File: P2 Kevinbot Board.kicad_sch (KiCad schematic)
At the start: 57 parts, among them J1 Screw_Terminal_01x02, J10 Conn_01x04, J11 Conn_01x04_Male, J12 Conn_02x06_Odd_Even, J13 Conn_01x04, J14 Conn_01x02, J15 Conn_01x04, J16 Conn_02x06_Odd_Even, J2 Conn_01x03_Male, J3 Screw_Terminal_01x02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

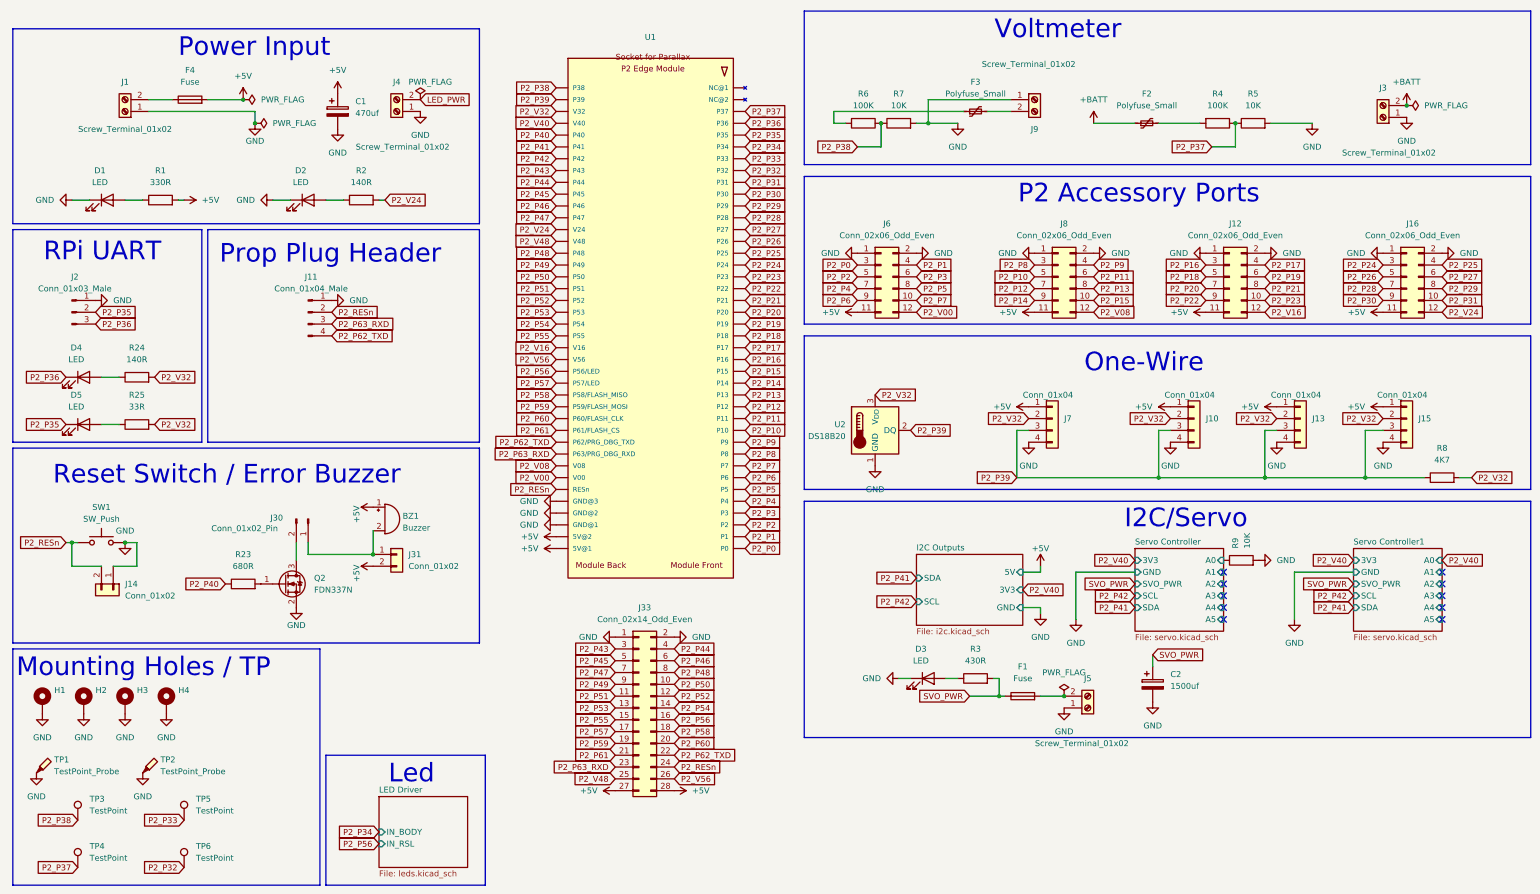
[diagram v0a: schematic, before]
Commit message: Remove all components, redo board outline
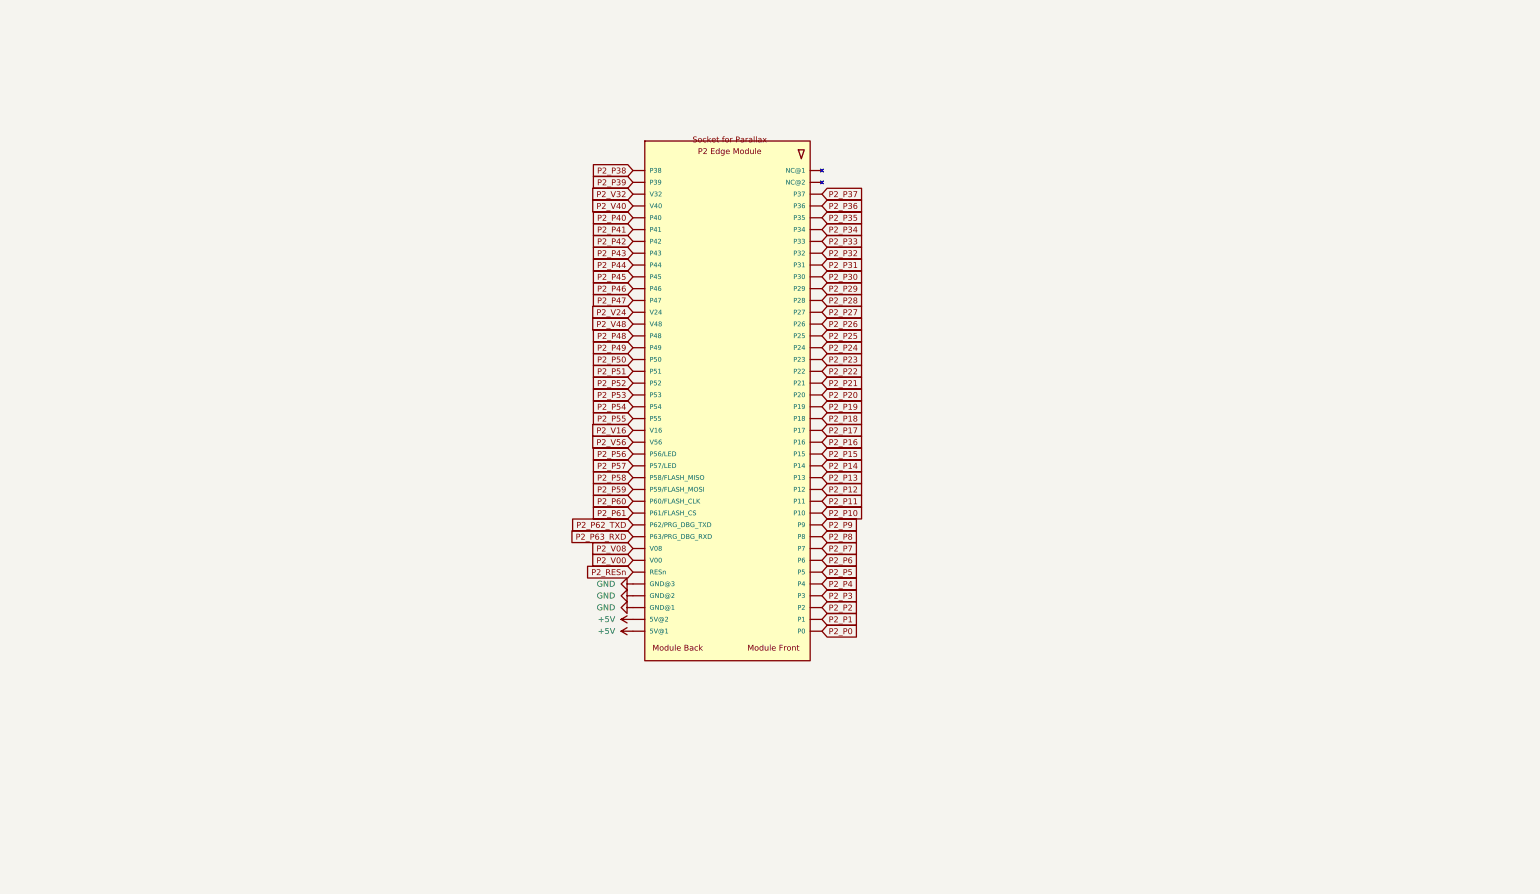
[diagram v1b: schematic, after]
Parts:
- removed BZ1: Buzzer, Buzzer_Beeper:Buzzer_TDK_PS1240P02BT_D12.2mm_H6.5mm, symbol Device:Buzzer
- removed C1: 470uf, Capacitor_THT:CP_Radial_D8.0mm_P3.50mm, symbol Device:C_Polarized
- removed C2: 1500uf, Capacitor_THT:CP_Radial_D8.0mm_P3.50mm, symbol Device:C_Polarized
- removed D1, D2, D3, D4, D5: LED, LED_SMD:LED_0805_2012Metric, symbol Device:LED
- removed F1, F4: Fuse, Fuse:Fuseholder_Blade_Mini_Keystone_3568, symbol Device:Fuse
- removed F2, F3: Polyfuse_Small, Fuse:Fuse_1206_3216Metric_Pad1.42x1.75mm_HandSolder, symbol Device:Polyfuse_Small
- removed H1, H2, H3, H4: MountingHole_Pad, MountingHole:MountingHole_3.5mm_Pad_TopBottom, symbol Mechanical:MountingHole_Pad
- removed J1, J3, J4, J5, J9: Screw_Terminal_01x02, Phoenix_MSTBA:MSTBA-2,5-2-G-5,08, symbol Connector:Screw_Terminal_01x02
- removed J10, J13, J15, J7: Conn_01x04, Connector_JST:JST_XH_B4B-XH-A_1x04_P2.50mm_Vertical, symbol Connector_Generic:Conn_01x04
- removed J11: Conn_01x04_Male, Connector_PinHeader_2.54mm:PinHeader_1x04_P2.54mm_Vertical, symbol Connector:Conn_01x04_Pin
- removed J12, J16, J6, J8: Conn_02x06_Odd_Even, Connector_PinHeader_2.54mm:PinHeader_2x06_P2.54mm_Vertical, symbol Connector_Generic:Conn_02x06_Odd_Even
- removed J14, J31: Conn_01x02, Connector_JST:JST_XH_B2B-XH-A_1x02_P2.50mm_Vertical, symbol Connector_Generic:Conn_01x02
- removed J2: Conn_01x03_Male, Connector_JST:JST_XH_B3B-XH-A_1x03_P2.50mm_Vertical, symbol Connector:Conn_01x03_Pin
- removed J30: Conn_01x02_Pin, Connector_PinHeader_2.54mm:PinHeader_1x02_P2.54mm_Vertical, symbol Connector:Conn_01x02_Pin
- removed J33: Conn_02x14_Odd_Even, Connector_FFC-FPC:TE_2-1734839-8_1x28-1MP_P0.5mm_Horizontal, symbol Connector_Generic:Conn_02x14_Odd_Even
- removed Q2: FDN337N, Package_TO_SOT_SMD:SOT-23-3, symbol Device:Q_NMOS_GSD
- removed R1: 330R, Resistor_SMD:R_0805_2012Metric, symbol Device:R
- removed R2, R24: 140R, Resistor_SMD:R_0805_2012Metric, symbol Device:R
- removed R23: 680R, Resistor_SMD:R_0603_1608Metric, symbol Device:R
- removed R25: 33R, Resistor_SMD:R_0805_2012Metric, symbol Device:R
- removed R3: 430R, Resistor_SMD:R_0805_2012Metric, symbol Device:R
- removed R4, R6: 100K, Resistor_THT:R_Axial_DIN0207_L6.3mm_D2.5mm_P10.16mm_Horizontal, symbol Device:R
- removed R5, R7: 10K, Resistor_THT:R_Axial_DIN0207_L6.3mm_D2.5mm_P10.16mm_Horizontal, symbol Device:R
- removed R8: 4K7, Resistor_SMD:R_0603_1608Metric, symbol Device:R
- removed R9: 10K, Resistor_SMD:R_0603_1608Metric, symbol Device:R
- removed SW1: SW_Push, Button_Switch_THT:SW_PUSH_6mm, symbol Switch:SW_Push
- removed TP1, TP2: TestPoint_Probe, Keystone:Keystone-1502-2, symbol Connector:TestPoint_Probe
- removed TP3, TP4, TP5, TP6: TestPoint, TestPoint:TestPoint_Pad_D1.0mm, symbol Connector:TestPoint
- removed U2: DS18B20, Package_TO_SOT_THT:TO-92_Inline_Wide, symbol Sensor_Temperature:DS18B20
- U1: footprint Parallax-P2:Card_Edge_SMT_VERT_1.27mm_80p -> Parallax-P2:Card_Edge_TH_RA_1.27mm_80p; Part Number 450-00309 -> (none)
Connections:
- no-connect marks 10 -> 0
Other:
- removed sheet I2C Outputs
- removed sheet LED Driver
- removed sheet Servo Controller
- removed sheet Servo Controller1
- note removed: "I2C/Servo"
- note removed: "Led"
- note removed: "Mounting Holes / TP"
- note removed: "One-Wire"
- note removed: "P2 Accessory Ports"
- note removed: "Power Input"
- note removed: "Prop Plug Header"
- note removed: "RPi UART"
- note removed: "Reset Switch / Error Buzzer"
- note removed: "Voltmeter"

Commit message: Mostly routed accessory headers
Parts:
- added J12, J16, J6, J8: Conn_02x06_Odd_Even, Connector_PinHeader_2.54mm:PinHeader_2x06_P2.54mm_Vertical, symbol Connector_Generic:Conn_02x06_Odd_Even
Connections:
- net +5V: now also J12.11 (Pin_11), J16.11 (Pin_11), J6.11 (Pin_11), J8.11 (Pin_11)
- net GND: now also J12.1 (Pin_1), J12.2 (Pin_2), J16.1 (Pin_1), J16.2 (Pin_2), J6.1 (Pin_1), J6.2 (Pin_2), J8.1 (Pin_1), J8.2 (Pin_2)
- net P2_P0: now also J6.3 (Pin_3)
- net P2_P1: now also J6.4 (Pin_4)
- net P2_P10: now also J8.5 (Pin_5)
- net P2_P11: now also J8.6 (Pin_6)
- net P2_P12: now also J8.7 (Pin_7)
- net P2_P13: now also J8.8 (Pin_8)
- net P2_P14: now also J8.9 (Pin_9)
- net P2_P15: now also J8.10 (Pin_10)
- net P2_P16: now also J12.3 (Pin_3)
- net P2_P17: now also J12.4 (Pin_4)
- net P2_P18: now also J12.5 (Pin_5)
- net P2_P19: now also J12.6 (Pin_6)
- net P2_P2: now also J6.5 (Pin_5)
- net P2_P20: now also J12.7 (Pin_7)
- net P2_P21: now also J12.8 (Pin_8)
- net P2_P22: now also J12.9 (Pin_9)
- net P2_P23: now also J12.10 (Pin_10)
- net P2_P24: now also J16.3 (Pin_3)
- net P2_P25: now also J16.4 (Pin_4)
- net P2_P26: now also J16.5 (Pin_5)
- net P2_P27: now also J16.6 (Pin_6)
- net P2_P28: now also J16.7 (Pin_7)
- net P2_P29: now also J16.8 (Pin_8)
- net P2_P3: now also J6.6 (Pin_6)
- net P2_P30: now also J16.9 (Pin_9)
- net P2_P31: now also J16.10 (Pin_10)
- net P2_P4: now also J6.7 (Pin_7)
- net P2_P5: now also J6.8 (Pin_8)
- net P2_P6: now also J6.9 (Pin_9)
- net P2_P7: now also J6.10 (Pin_10)
- net P2_P8: now also J8.3 (Pin_3)
- net P2_P9: now also J8.4 (Pin_4)
- net P2_V00: now also J6.12 (Pin_12)
- net P2_V08: now also J8.12 (Pin_12)
- net P2_V16: now also J12.12 (Pin_12)
- net P2_V24: now also J16.12 (Pin_12)

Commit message: Begin work on usbc programmer, misc
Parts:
- added J1, J2: Conn_01x03_Pin, Connector_PinHeader_2.54mm:PinHeader_1x03_P2.54mm_Vertical, symbol Connector:Conn_01x03_Pin
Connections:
- net +5V: now also J1.1 (Pin_1), J2.1 (Pin_1); no longer J12.11 (Pin_11), J16.11 (Pin_11), J6.11 (Pin_11), J8.11 (Pin_11)
- new net: J12.11 (Pin_11), J16.11 (Pin_11), J2.2 (Pin_2)
- new net: J1.2 (Pin_2), J6.11 (Pin_11), J8.11 (Pin_11)
- no-connect marks 0 -> 2
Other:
- added sheet Programmer (prog.kicad_sch)

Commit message: Usb programme
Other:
- sheet Programmer ports: added RESn, RX, TX; removed none
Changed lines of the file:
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@@
 	(wire
 		(pts
+			(xy 39.37 147.32) (xy 49.53 147.32)
+		)
+		(stroke
+			(width 0)
+			(type default)
+		)
+	)
+	(wire
+		(pts
 			(xy 171.45 147.32) (xy 171.45 158.75)
 		)
@@
 	(wire
 		(pts
+			(xy 162.56 88.9) (xy 163.83 88.9)
+		)
+		(stroke
+			(width 0)
+			(type default)
+		)
+	)
+	(wire
+		(pts
 			(xy 284.48 147.32) (xy 284.48 130.81)
 		)
@@
 		)
 	)
+	(label "P2_RESn"
+		(at 162.56 88.9 180)
+		(effects
+			(font
+				(size 1.27 1.27)
+			)
+			(justify right bottom)
+		)
+	)
+	(label "P2_RESn"
+		(at 39.37 147.32 180)
+		(effects
+			(font
+				(size 1.27 1.27)
+			)
+			(justify right bottom)
+		)
+	)
 	(global_label "P2_P31"
 		(shape input)
@@
 		)
 	)
-	(global_label "P2_RESn"
-		(shape input)
-		(at 49.53 147.32 180)
-		(fields_autoplaced yes)
-		(effects
-			(font
-				(size 1.27 1.27)
-			)
-			(justify right)
-		)
-		(property "Intersheetrefs" "${INTERSHEET_REFS}"
-			(at 38.8921 147.2406 0)
-			(effects
-				(font
-					(size 1.27 1.27)
-				)
-				(justify right)
-				(hide yes)
-			)
-		)
-	)
 	(global_label "P2_P16"
 		(shape input)
@@
 		)
 	)
+	(global_label "P2_P62_TXD"
+		(shape input)
+		(at 163.83 91.44 180)
+		(fields_autoplaced yes)
+		(effects
+			(font
+				(size 1.27 1.27)
+			)
+			(justify right)
+		)
+		(property "Intersheetrefs" "${INTERSHEET_REFS}"
+			(at 149.8659 91.5194 0)
+			(effects
+				(font
+					(size 1.27 1.27)
+				)
+				(justify right)
+				(hide yes)
+			)
+		)
+	)
+	(global_label "P2_P63_RXD"
+		(shape input)
+		(at 163.83 93.98 180)
+		(fields_autoplaced yes)
+		(effects
+			(font
+				(size 1.27 1.27)
+			)
+			(justify right)
+		)
+		(property "Intersheetrefs" "${INTERSHEET_REFS}"
+			(at 149.5636 94.0594 0)
+			(effects
+				(font
+					(size 1.27 1.27)
+				)
+				(justify right)
+				(hide yes)
+			)
+		)
+	)
 	(global_label "P2_P7"
 		(shape input)
@@
 	)
 	(sheet
-		(at 185.42 171.45)
-		(size 36.83 16.51)
+		(at 163.83 83.82)
+		(size 20.32 15.24)
 		(exclude_from_sim no)
 		(in_bom yes)
@@
 		)
 		(property "Sheetname" "Programmer"
-			(at 185.42 170.7384 0)
+			(at 163.83 83.1084 0)
 			(effects
 				(font
@@
 		)
 		(property "Sheetfile" "prog.kicad_sch"
-			(at 185.42 188.5446 0)
+			(at 163.83 99.6446 0)
 			(effects
 				(font
@@
 			)
 		)
+		(pin "RESn" input
+			(at 163.83 88.9 180)
+			(effects
+				(font
+					(size 1.27 1.27)
+				)
+				(justify left)
+			)
+		)
+		(pin "RX" input
+			(at 163.83 91.44 180)
+			(effects
+				(font
+					(size 1.27 1.27)
+				)
+				(justify left)
+			)
+		)
+		(pin "TX" input
+			(at 163.83 93.98 180)
+			(effects
+				(font
+					(size 1.27 1.27)
+				)
+				(justify left)
+			)
+		)

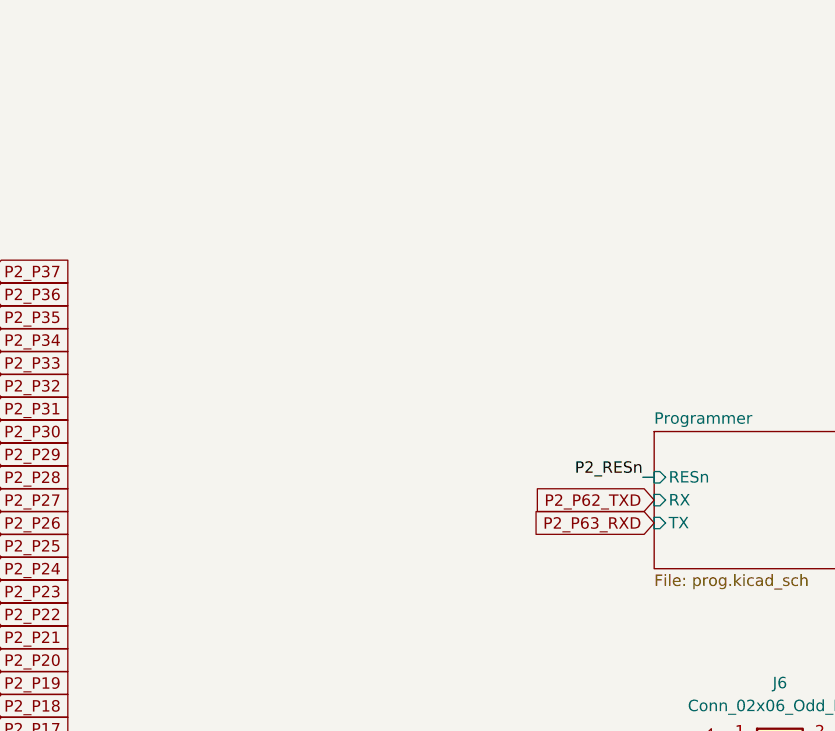
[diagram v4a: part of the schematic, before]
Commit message: Place buzzer
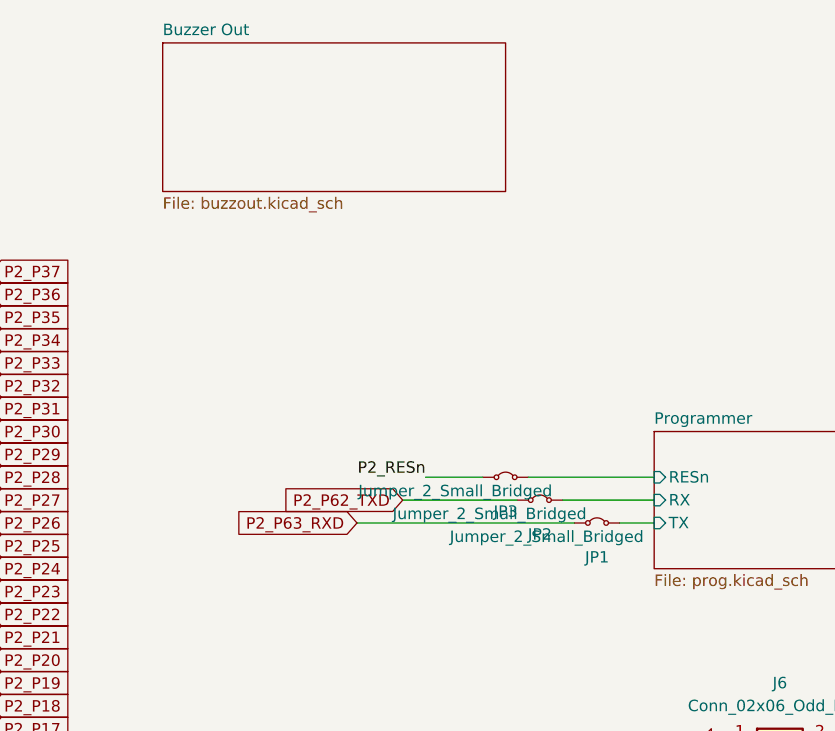
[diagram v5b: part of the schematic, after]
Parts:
- added JP1, JP2, JP3: Jumper_2_Small_Bridged, Jumper:SolderJumper-2_P1.3mm_Bridged_RoundedPad1.0x1.5mm, symbol Jumper:Jumper_2_Small_Bridged
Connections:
- net P2_P62_TXD: now also JP2.1 (A)
- net P2_P63_RXD: now also JP1.1 (A)
- net P2_RESn: now also JP3.1 (A)
- new net Programmer/RESn: JP3.2 (B)
- new net Programmer/RX: JP2.2 (B)
- new net Programmer/TX: JP1.2 (B)
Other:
- added sheet Buzzer Out (buzzout.kicad_sch)

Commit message: Buzzer
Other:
- sheet Buzzer Out ports: added SIG, VIN; removed none
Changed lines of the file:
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@@
+		)
+	)
+	(global_label "P2_P34"
+		(shape input)
+		(at 163.83 68.58 180)
+		(fields_autoplaced yes)
+		(effects
+			(font
+				(size 1.27 1.27)
+			)
+			(justify right)
+		)
+		(property "Intersheetrefs" "${INTERSHEET_REFS}"
+			(at 153.7087 68.58 0)
+			(effects
+				(font
+					(size 1.27 1.27)
+				)
+				(justify right)
+				(hide yes)
+			)
 		)
 	)
@@
 		)
 	)
+	(symbol
+		(lib_id "power:+5V")
+		(at 163.83 66.04 90)
+		(unit 1)
+		(exclude_from_sim no)
+		(in_bom yes)
+		(on_board yes)
+		(dnp no)
+		(fields_autoplaced yes)
+		(property "Reference" "#PWR028"
+			(at 167.64 66.04 0)
+			(effects
+				(font
+					(size 1.27 1.27)
+				)
+				(hide yes)
+			)
+		)
+		(property "Value" "+5V"
+			(at 160.02 66.0399 90)
+			(effects
+				(font
+					(size 1.27 1.27)
+				)
+				(justify left)
+			)
+		)
+		(property "Footprint" ""
+			(at 163.83 66.04 0)
+			(effects
+				(font
+					(size 1.27 1.27)
+				)
+				(hide yes)
+			)
+		)
+		(property "Datasheet" ""
+			(at 163.83 66.04 0)
+			(effects
+				(font
+					(size 1.27 1.27)
+				)
+				(hide yes)
+			)
+		)
+		(property "Description" "Power symbol creates a global label with name \"+5V\""
+			(at 163.83 66.04 0)
+			(effects
+				(font
+					(size 1.27 1.27)
+				)
+				(hide yes)
+			)
+		)
+		(pin "1"
+		)
+		(instances
+			(project "P2 Kevinbot Board"
+				(path "/362ca48c-0b77-4943-b8b3-fc15ab97f30d"
+					(reference "#PWR028")
+					(unit 1)
+				)
+			)
+		)
+	)
 	(sheet
-		(at 109.22 40.64)
-		(size 38.1 16.51)
+		(at 163.83 59.69)
+		(size 20.32 16.51)
 		(exclude_from_sim no)
 		(in_bom yes)
@@
 		)
 		(property "Sheetname" "Buzzer Out"
-			(at 109.22 39.9284 0)
+			(at 163.83 58.9784 0)
 			(effects
 				(font
@@
 		)
 		(property "Sheetfile" "buzzout.kicad_sch"
-			(at 109.22 57.7346 0)
+			(at 163.83 76.7846 0)
 			(effects
 				(font
@@
 			)
 		)
+		(pin "SIG" input
+			(at 163.83 68.58 180)
+			(effects
+				(font
+					(size 1.27 1.27)
+				)
+				(justify left)
+			)
+		)
+		(pin "VIN" input
+			(at 163.83 66.04 180)
+			(effects
+				(font
+					(size 1.27 1.27)
+				)
+				(justify left)
+			)
+		)
